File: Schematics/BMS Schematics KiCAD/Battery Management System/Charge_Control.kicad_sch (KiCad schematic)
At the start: 43 parts, among them Q15 2N7002, Q16 2N7002, Q17 2N7002, Q21 2N7002, Q22 BSD235C, U3 BQ25730RSNR

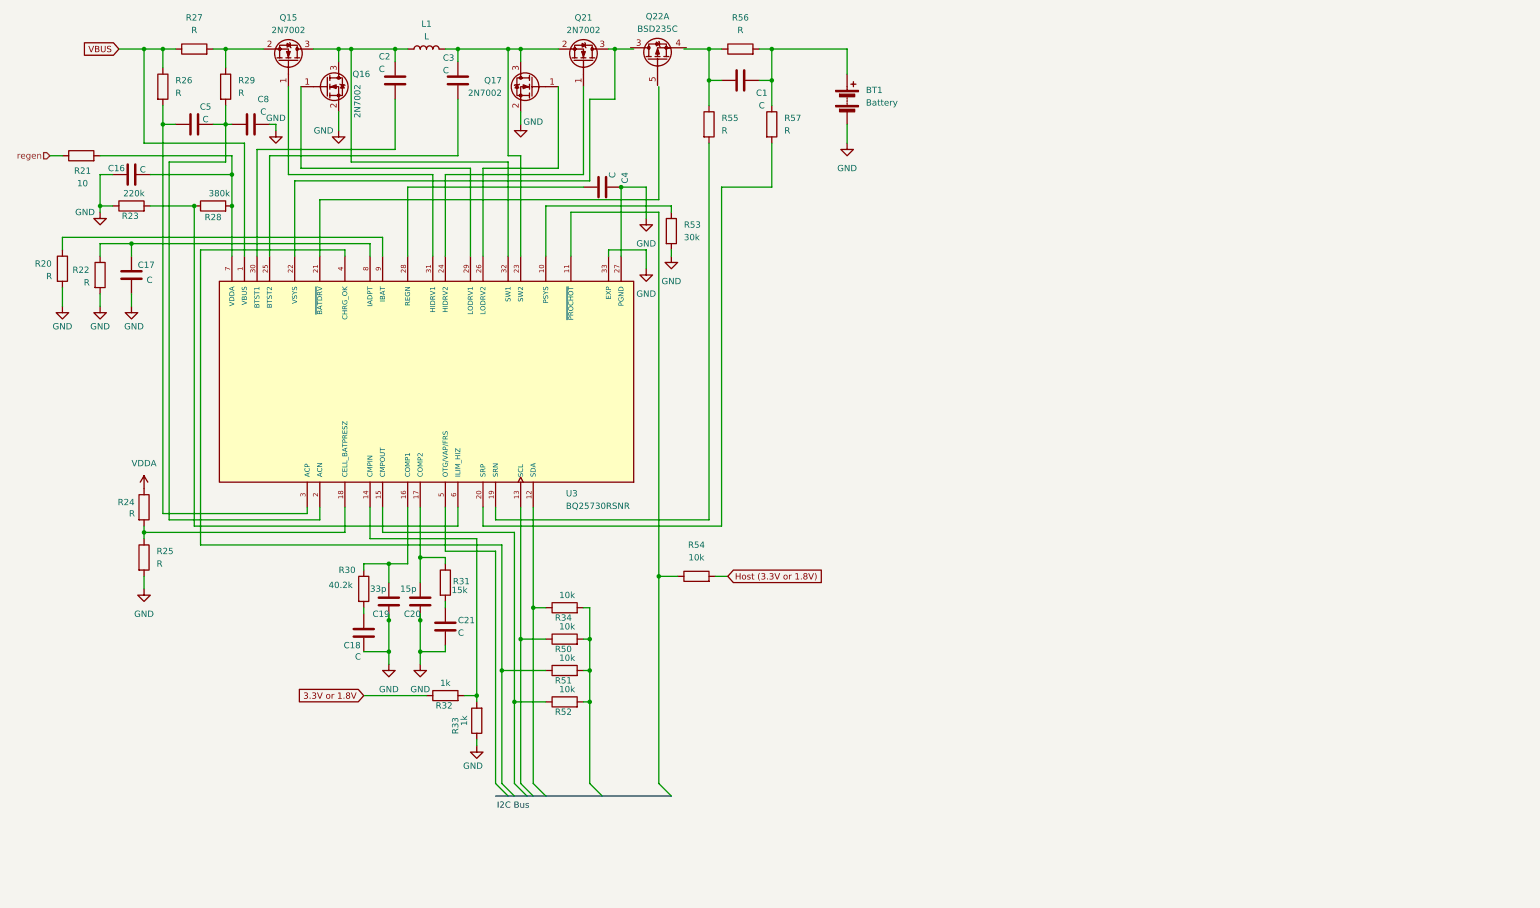
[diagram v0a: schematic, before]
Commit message: Add files via upload
Latest iteration of KiCAD schematic for Battery Management System
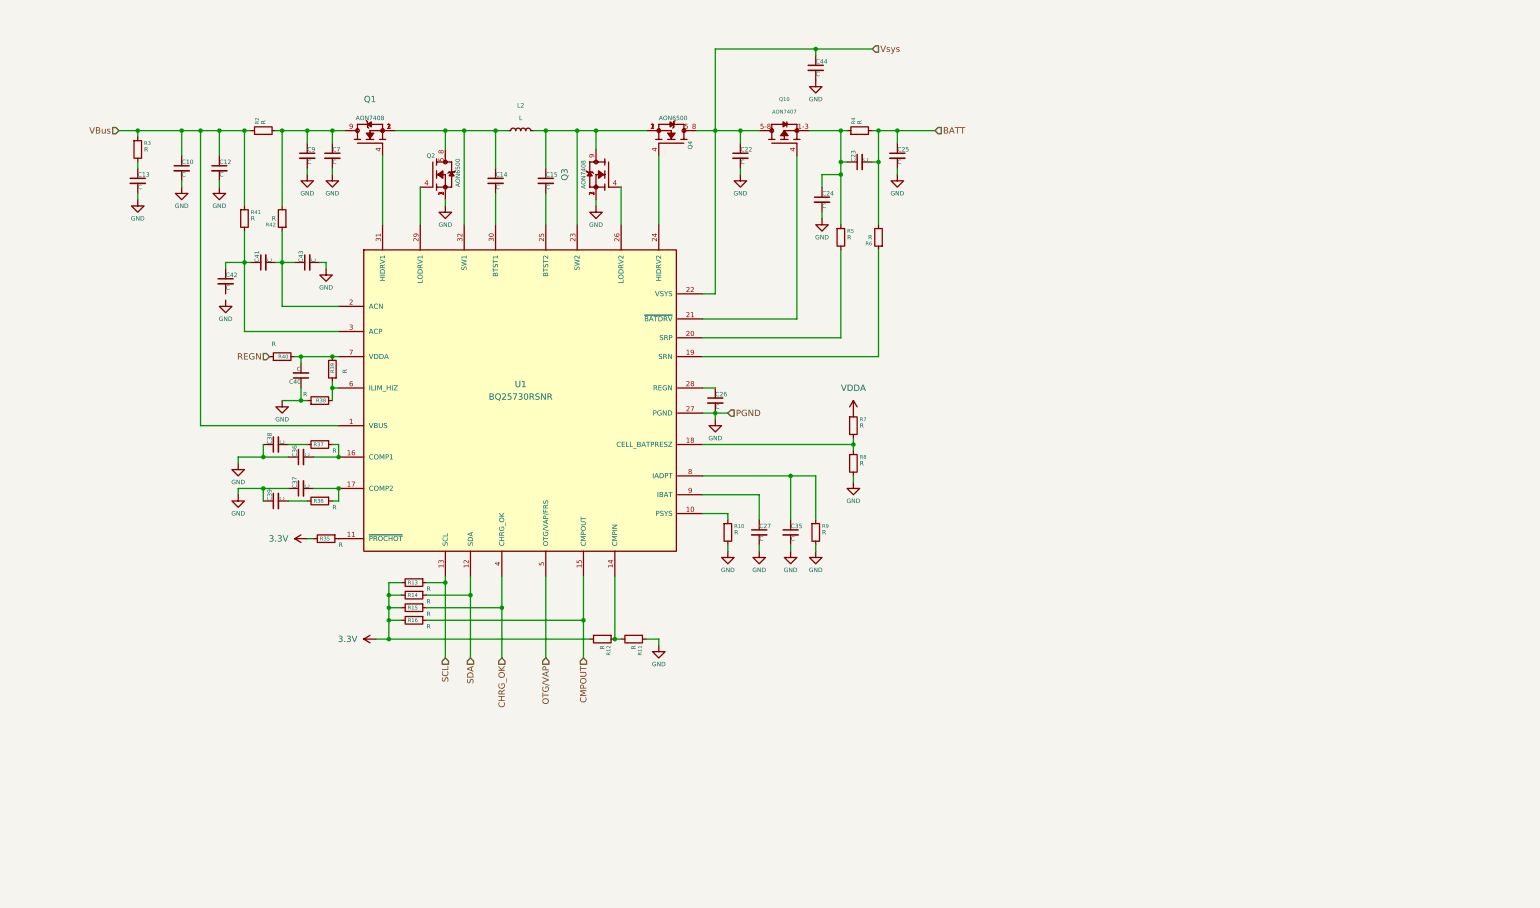
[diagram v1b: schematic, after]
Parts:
- removed BT1: Battery, symbol Device:Battery
- removed C1, C17, C18, C2, C21, C3, C4, C5, C8: C, Resistor_SMD:R_0201_0603Metric, symbol Device:C
- removed C16: C, symbol Device:C
- removed C19: 33p, Resistor_SMD:R_0201_0603Metric, symbol Device:C
- removed C20: 15p, Resistor_SMD:R_0201_0603Metric, symbol Device:C
- removed L1: L, symbol Device:L
- removed Q15, Q16, Q17, Q21: 2N7002, Package_TO_SOT_SMD:SOT-23, symbol Transistor_FET:2N7002
- removed Q22: BSD235C, Package_TO_SOT_SMD:SOT-363_SC-70-6, symbol Transistor_FET:BSD235C
- removed R20, R22, R24, R25, R26, R27, R29, R55, R56, R57: R, Resistor_SMD:R_0201_0603Metric, symbol Device:R
- removed R21: 10, Resistor_SMD:R_0201_0603Metric, symbol Device:R
- removed R23: 220k, Resistor_SMD:R_0201_0603Metric, symbol Device:R
- removed R28: 380k, Resistor_SMD:R_0201_0603Metric, symbol Device:R
- removed R30: 40.2k, Resistor_SMD:R_0201_0603Metric, symbol Device:R
- removed R31: 15k, Resistor_SMD:R_0201_0603Metric, symbol Device:R
- removed R32, R33: 1k, Resistor_SMD:R_0201_0603Metric, symbol Device:R
- removed R34, R50, R51, R52, R54: 10k, Resistor_SMD:R_0201_0603Metric, symbol Device:R
- removed R53: 30k, Resistor_SMD:R_0201_0603Metric, symbol Device:R
- removed U3: BQ25730RSNR, BQ25730RSNR:IC_BQ25730RSNR, symbol BQ25730RSNR:BQ25730RSNR
- added C10, C12, C13, C14, C15, C22, C23, C24, C25, C26, C27, C35, C36, C37, C38, C39, C40, C41, C42, C43, C44, C7, C9: C, symbol Device:C_Small
- added L2: L, symbol Device:L_Small
- added Q1, Q3: AON7408, AON7408:TRANS_AON7408, symbol AON7408:AON7408
- added Q10: AON7407, AON7407:TRANS_AON7407, symbol AON7407:AON7407
- added Q2, Q4: AON6500, AON6500:TRANS_AON6500, symbol AON6500:AON6500
- added R10, R11, R12, R13, R14, R15, R16, R2, R3, R35, R36, R37, R38, R39, R4, R40, R41, R42, R5, R6, R7, R8, R9: R, symbol Device:R_Small
- added U1: BQ25730RSNR, BQ25730RSNR:IC_BQ25730RSNR, symbol BQ25730RSNR:BQ25730RSNR
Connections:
- net GND: now also C10.2, C12.2, C13.2, C22.2, C24.2, C25.2, C26.2, C27.2, C35.2, C36.1, C37.1, C38.1, C39.1, C40.1, C43.2, C44.2, C7.2, C9.2, Q2.1, Q2.2, Q2.3, Q3.1, Q3.2, Q3.3, R10.2, R11.1, R38.1, R8.2, R9.2, U1.27 (PGND)
- net VDDA: now also R7.1
- new net: R10.1, U1.10 (PSYS)
- new net: R35.1, U1.11 (~{PROCHOT})
- new net: R11.2, R12.1, U1.14 (CMPIN)
- new net: C36.2, R37.1, U1.16 (COMP1)
- new net: C37.2, R36.1, U1.17 (COMP2)
- new net: R7.2, R8.1, U1.18 (CELL_BATPRESZ)
- new net: R6.1, U1.19 (SRN)
- new net: C41.2, C43.1, R42.1, U1.2 (ACN)
- new net: R5.2, U1.20 (SRP)
- new net: Q10.4, U1.21 (~{BATDRV})
- new net: C15.1, L2.2, Q3.9, Q4.1, Q4.2, Q4.3, U1.23 (SW2)
- new net: Q4.4, U1.24 (HIDRV2)
- new net: C15.2, U1.25 (BTST2)
- new net: Q3.4, U1.26 (LODRV2)
- new net: C26.1, U1.28 (REGN)
- new net: Q2.4, U1.29 (LODRV1)
- new net: C41.1, C42.1, R41.2, U1.3 (ACP)
- new net: C14.2, U1.30 (BTST1)
- new net: Q1.4, U1.31 (HIDRV1)
- new net: C14.1, L2.1, Q1.1, Q1.2, Q1.3, Q2.5_8, U1.32 (SW1)
- new net: R38.2, R39.1, U1.6 (ILIM_HIZ)
- new net: C40.2, R39.2, R40.2, U1.7 (VDDA)
- new net: C35.1, R9.1, U1.8 (IADPT)
- new net: C27.1, U1.9 (IBAT)
- new net: C39.2, R36.2
- new net: C7.1, C9.1, Q1.9, R2.2, R42.2
- new net: C13.1, R3.2
- new net: C23.1, C24.1, Q10.1-3, R4.1, R5.1
- new net: C38.2, R37.2
- new net 3.3V: R12.2, R13.2, R14.2, R15.2, R16.2, R35.2
- new net BATT: C23.2, C25.1, R4.2, R6.2
- new net CHRG_OK: R15.1, U1.4 (CHRG_OK)
- new net CMPOUT: R16.1, U1.15 (CMPOUT)
- new net OTG/VAP: U1.5 (OTG/VAP/FRS)
- new net REGN: R40.1
- new net SCL: R13.1, U1.13 (SCL)
- new net SDA: R14.1, U1.12 (SDA)
- new net VBus: C10.1, C12.1, R2.1, R3.1, R41.1, U1.1 (VBUS)
- new net Vsys: C22.1, C44.1, Q10.5-8, Q4.5_8, U1.22 (VSYS)
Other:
- note removed: "I2C Bus"
- title: Battery management System - Charge Controller -> Battery Management System

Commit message: Pulled together root sheet so that it's obvious how the power flows and how the blocks are connected. Finally, a decent block diagram :)
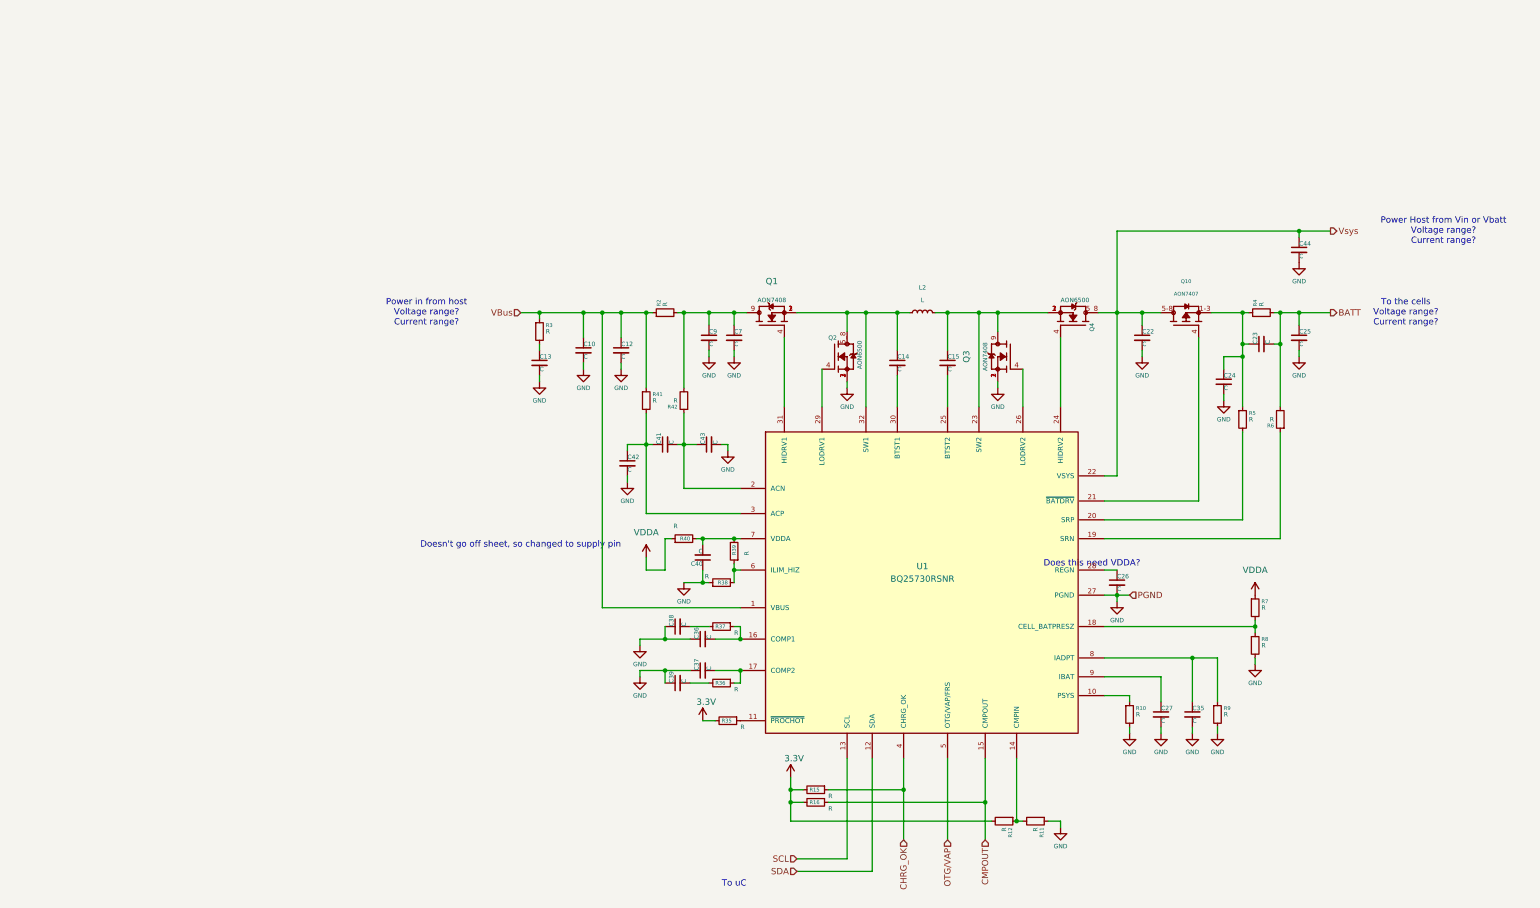
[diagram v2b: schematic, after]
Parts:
- removed R13, R14: R, symbol Device:R_Small
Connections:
- net REGN is gone; now on net VDDA: R40.1
- net GND: now also C42.2
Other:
- note added: "Does this need VDDA?"
- note added: "Doesn't go off sheet, so changed to supply pin"
- note added: "Power Host from Vin or Vbatt Voltage range? Current range?"
- note added: "Power in from host Voltage range? Current range?"
- note added: "To the cells Voltage range? Current range?"
- note added: "To uC"
- moved on the sheet: C10, C12, C13, C14, C15, C22, C23, C24, C25, C26, C27, C35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
